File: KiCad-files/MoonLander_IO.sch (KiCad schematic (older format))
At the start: 5 parts, among them P4 CONN_02X08, SW1 SW_PUSH, SW2 SW_PUSH

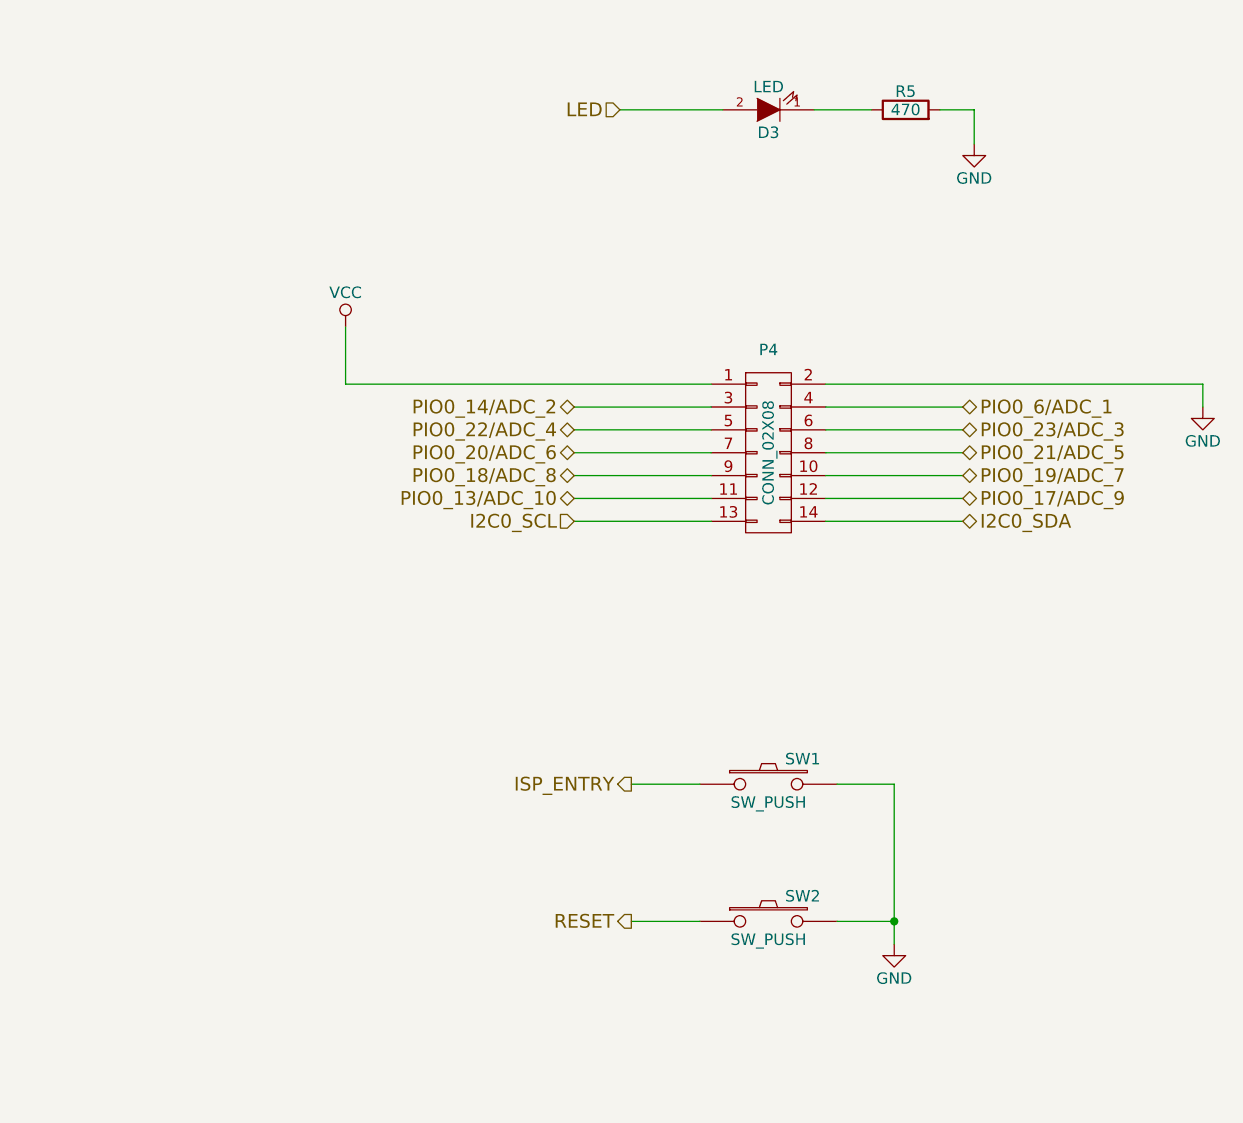
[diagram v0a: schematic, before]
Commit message: added I2C EEPROM, redid ground stitching
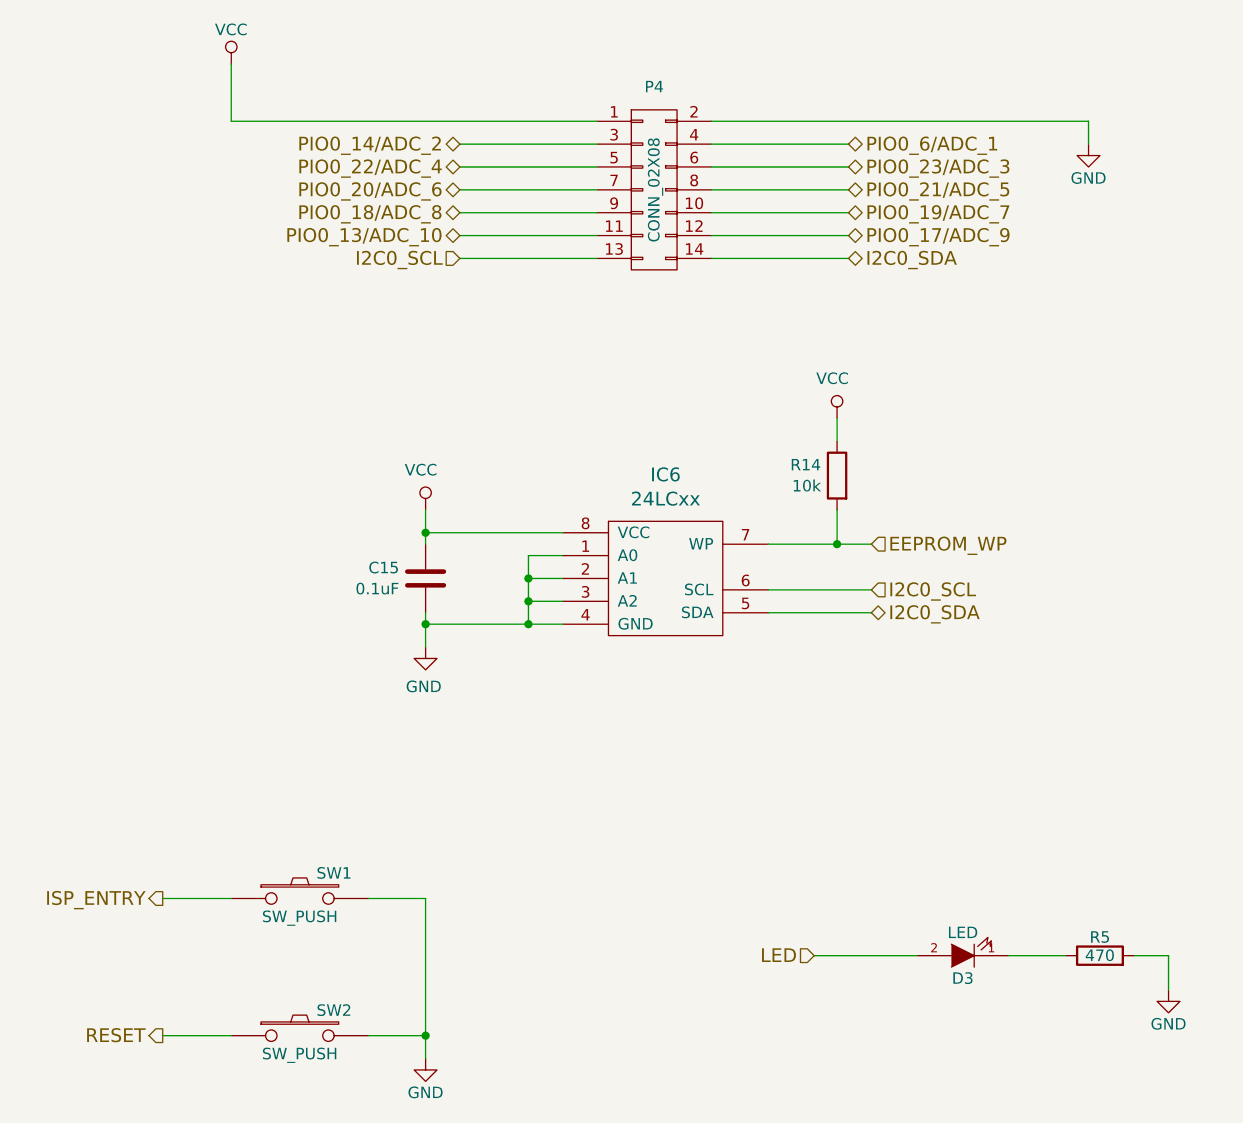
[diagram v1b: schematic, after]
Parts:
- added C15: 0.1uF, Capacitors_SMD:C_0402, symbol C
- added IC6: 24LCxx, Housings_DFN_QFN:DFN-8-1EP_2x2mm_Pitch0.5mm, symbol 24LCxx
- added R14: 10k, Resistors_SMD:R_0402, symbol R
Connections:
- net GND: now also C15.2, IC6.1 (A0), IC6.2 (A1), IC6.3 (A2), IC6.4 (GND)
- net I2C0_SCL: now also IC6.6 (SCL)
- net I2C0_SDA: now also IC6.5 (SDA)
- net VCC: now also C15.1, IC6.8 (VCC), R14.1
- new net EEPROM_WP: IC6.7 (WP), R14.2
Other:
- moved on the sheet: D3, P4, R5, SW1, SW2

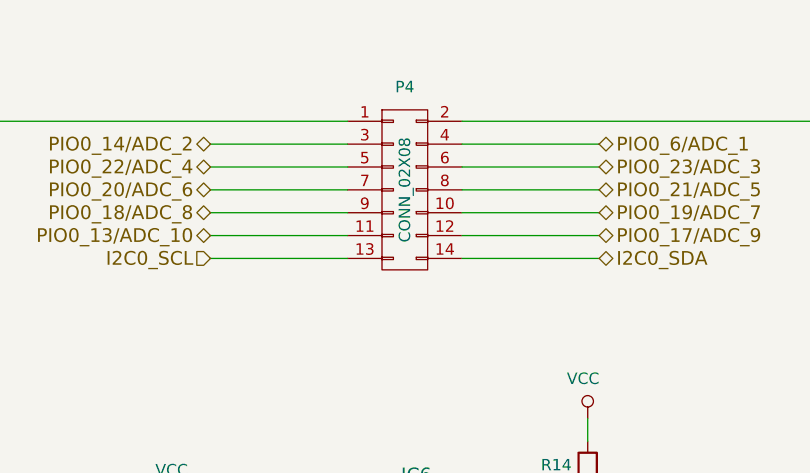
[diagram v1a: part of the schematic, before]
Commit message: fixed header symbol/footprint naming, minor changes
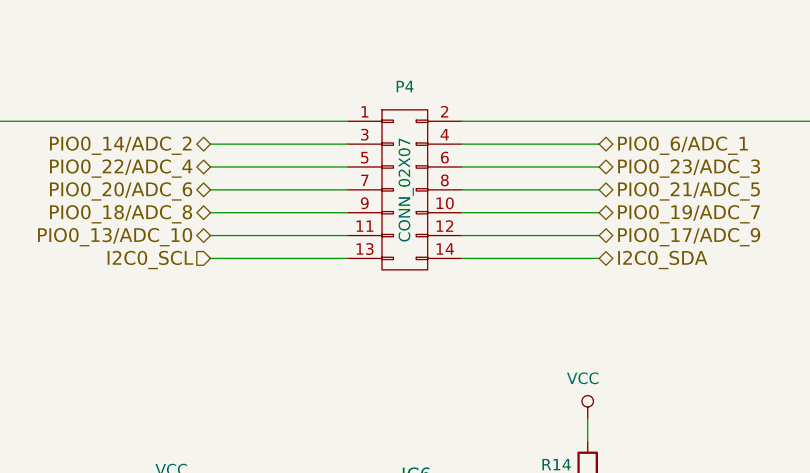
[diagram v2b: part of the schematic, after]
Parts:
- P4: value CONN_02X08 -> CONN_02X07; footprint GrayCatLabs:Header_2mm_2x6 -> GrayCatLabs:Header_2mm_2x7
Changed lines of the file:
@@
 P 5650 2000
 F 0 "P4" H 5650 2450 50  0000 C CNN
-F 1 "CONN_02X08" V 5650 2000 50  0000 C CNN
-F 2 "GrayCatLabs:Header_2mm_2x6" H 5650 800 50  0001 C CNN
+F 1 "CONN_02X07" V 5650 2000 50  0000 C CNN
+F 2 "GrayCatLabs:Header_2mm_2x7" H 5650 800 50  0001 C CNN
 F 3 "" H 5650 800 50  0000 C CNN
 	1    5650 2000
@@
 03 43 83 61 8C 09 03 03 03 03 43 83 61 8C 09 03 03 03 03 43 83 61 8C 09 03 03 03 03 43 83 61 03
 60 D2 64 32 30 30 30 30 34 84 CF 1C 00 A9 00 9C 01 A8 8B 59 19 06 06 06 06 06 E9 E3 33 80 C5 FF
-07 47 25 A5 D2 E9 03 52 D8 00 00 00 00 49 45 4E 44 AE 42 60 82 7F
+07 47 25 A5 D2 E9 03 52 D8 00 00 00 00 49 45 4E 44 AE 42 60 82 00
 EndData
 $EndBitmap

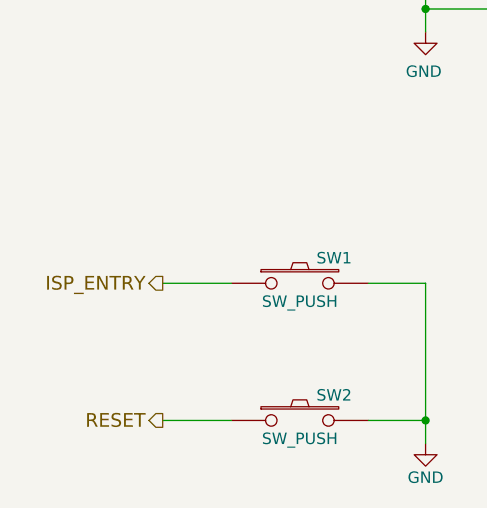
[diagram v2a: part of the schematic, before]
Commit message: drive ISP_ENTRY and RST from CP2110 GPIO outputs
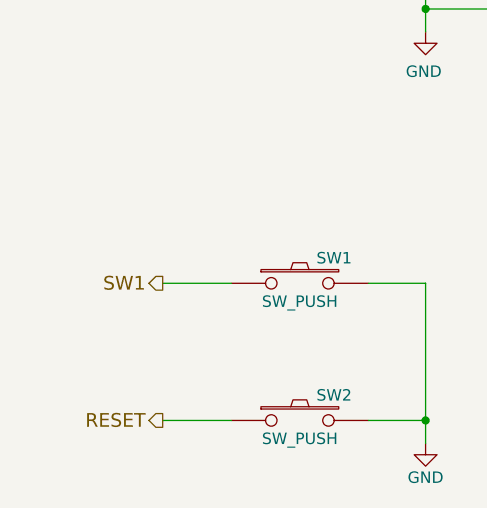
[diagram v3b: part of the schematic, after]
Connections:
- net ISP_ENTRY renamed SW1
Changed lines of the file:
@@
 I2C0_SDA
 Text HLabel 3500 5100 0    60   Output ~ 0
-ISP_ENTRY
+SW1
 $Comp
 L SW_PUSH SW1
@@
 PIO0_23/ADC_3
 $Comp
-L VCC #PWR8
+L VCC #PWR7
 U 1 1 56611529
 P 3800 1450
-F 0 "#PWR8" H 3800 1300 50  0001 C CNN
+F 0 "#PWR7" H 3800 1300 50  0001 C CNN
 F 1 "VCC" H 3800 1600 50  0000 C CNN
 F 2 "" H 3800 1450 50  0000 C CNN
@@
 $EndComp
 $Comp
-L GND #PWR25
+L GND #PWR24
 U 1 1 5661153F
 P 7550 1800
-F 0 "#PWR25" H 7550 1550 50  0001 C CNN
+F 0 "#PWR24" H 7550 1550 50  0001 C CNN
 F 1 "GND" H 7550 1650 50  0000 C CNN
 F 2 "" H 7550 1800 50  0000 C CNN
@@
 $EndComp
 $Comp
-L GND #PWR15
+L GND #PWR14
 U 1 1 565FFC9F
 P 4650 5800
-F 0 "#PWR15" H 4650 5550 50  0001 C CNN
+F 0 "#PWR14" H 4650 5550 50  0001 C CNN
 F 1 "GND" H 4650 5650 50  0000 C CNN
 F 2 "" H 4650 5800 50  0000 C CNN
@@
 $EndComp
 $Comp
-L GND #PWR27
+L GND #PWR26
 U 1 1 56655DF9
 P 7900 5500
-F 0 "#PWR27" H 7900 5250 50  0001 C CNN
+F 0 "#PWR26" H 7900 5250 50  0001 C CNN
 F 1 "GND" H 7900 5350 50  0000 C CNN
 F 2 "" H 7900 5500 50  0000 C CNN
@@
 03 43 83 61 8C 09 03 03 03 03 43 83 61 8C 09 03 03 03 03 43 83 61 8C 09 03 03 03 03 43 83 61 03
 60 D2 64 32 30 30 30 30 34 84 CF 1C 00 A9 00 9C 01 A8 8B 59 19 06 06 06 06 06 E9 E3 33 80 C5 FF
-07 47 25 A5 D2 E9 03 52 D8 00 00 00 00 49 45 4E 44 AE 42 60 82 00
+07 47 25 A5 D2 E9 03 52 D8 00 00 00 00 49 45 4E 44 AE 42 60 82 7F
 EndData
 $EndBitmap
@@
 $EndComp
 $Comp
-L VCC #PWR21
+L VCC #PWR20
 U 1 1 569ECAC0
 P 6450 3000
-F 0 "#PWR21" H 6450 2850 50  0001 C CNN
+F 0 "#PWR20" H 6450 2850 50  0001 C CNN
 F 1 "VCC" H 6470 3174 50  0000 C CNN
 F 2 "" H 6450 3000 50  0000 C CNN
@@
 $EndComp
 $Comp
-L VCC #PWR13
+L VCC #PWR12
 U 1 1 569ECAFA
 P 4650 3400
-F 0 "#PWR13" H 4650 3250 50  0001 C CNN
+F 0 "#PWR12" H 4650 3250 50  0001 C CNN
 F 1 "VCC" H 4670 3574 50  0000 C CNN
 F 2 "" H 4650 3400 50  0000 C CNN
@@
 $EndComp
 $Comp
-L GND #PWR14
+L GND #PWR13
 U 1 1 569ECB30
 P 4650 4000
-F 0 "#PWR14" H 4650 3750 50  0001 C CNN
+F 0 "#PWR13" H 4650 3750 50  0001 C CNN
 F 1 "GND" H 4658 3826 50  0000 C CNN
 F 2 "" H 4650 4000 50  0000 C CNN
